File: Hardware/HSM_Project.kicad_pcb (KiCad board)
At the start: 2 copper layers, 100.6 x 113.7 mm, 105 parts, among them J1 Conn_01x02_Pin, J10 VL530X Connector, J11 VL530X Connector, J12 VL530X Connector, J13 VL530X Connector, J14 BNO085 Breakout, J16 HC-05 Breakout Board, J2 MP1584 Breakout, J4 TEENSY_4.1, J5 Conn_01x08_Pin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

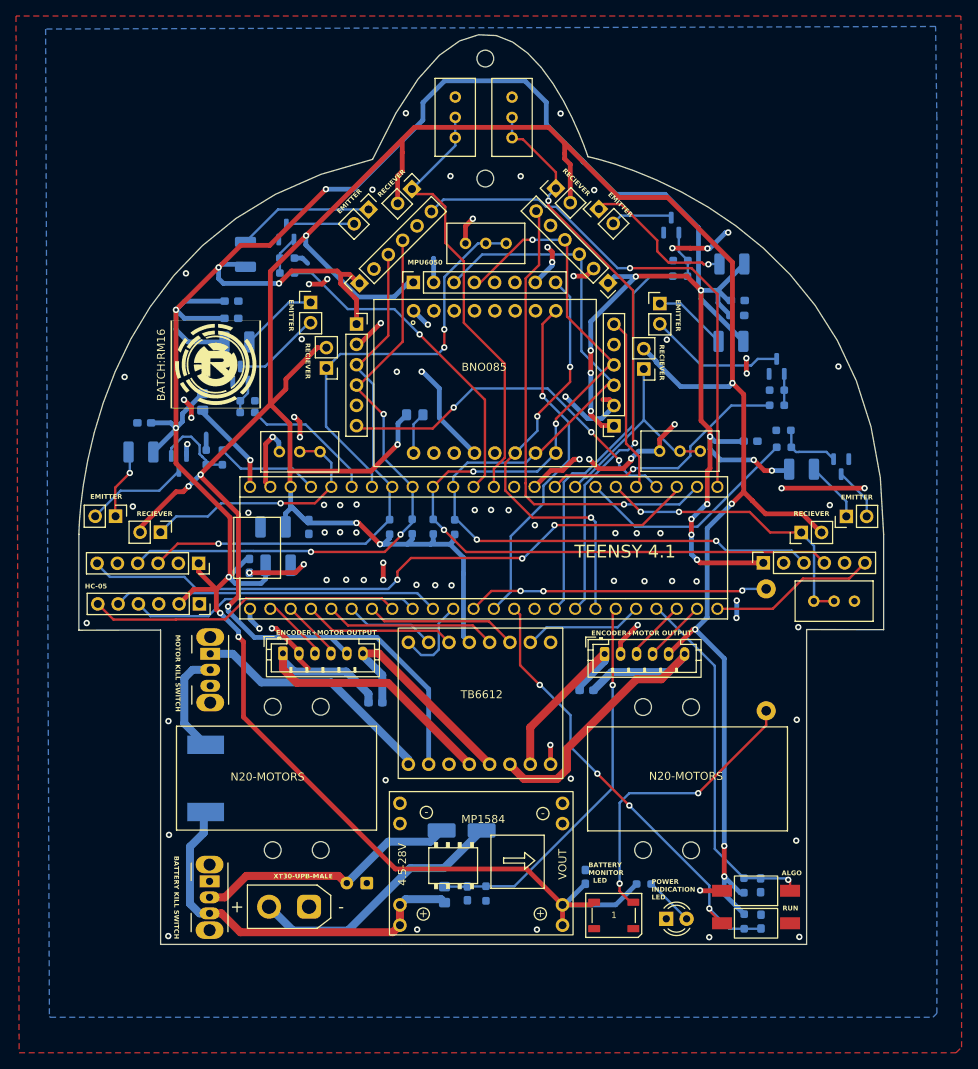
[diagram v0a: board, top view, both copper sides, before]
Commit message: Clean repository and update PCB design
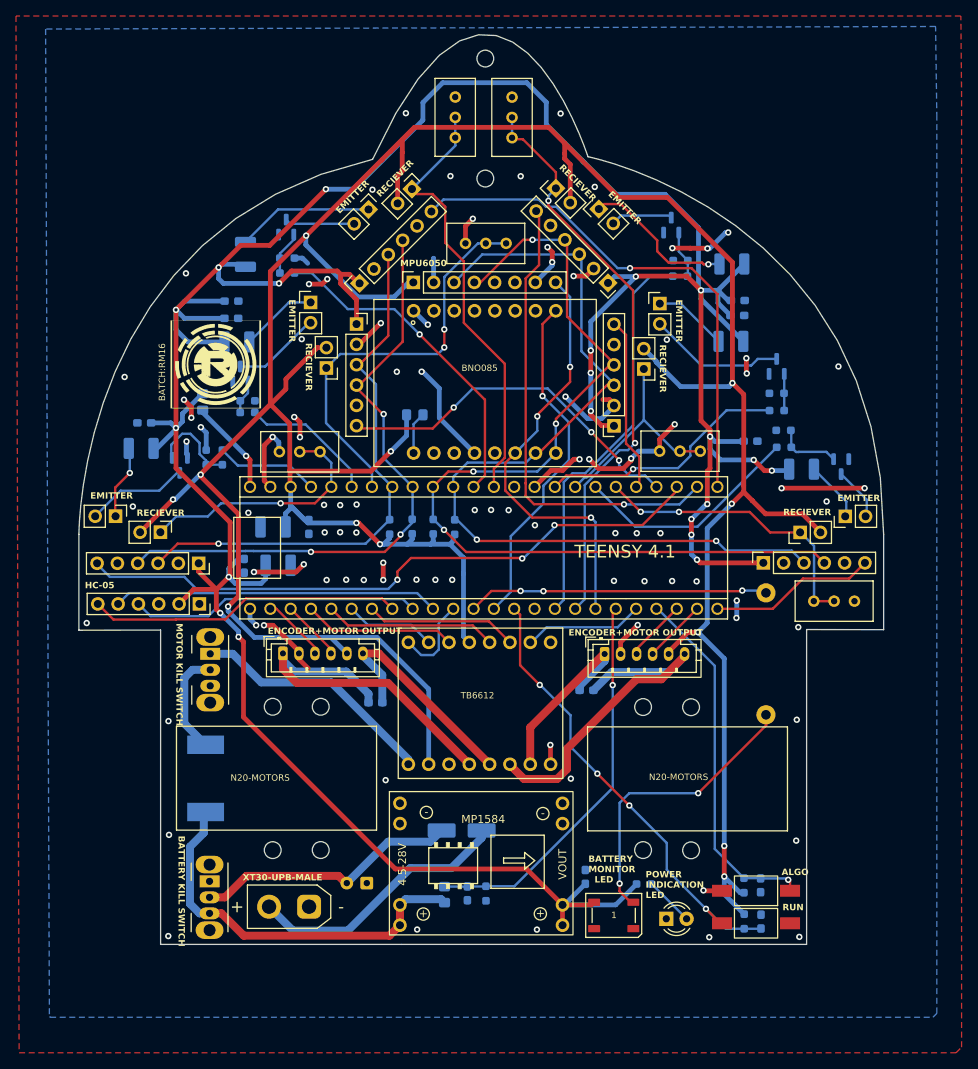
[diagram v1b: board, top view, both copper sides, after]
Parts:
- moved R19 0.66 mm to (190.2, 64.6)
- moved C4 0.65 mm to (123.6, 84.0)
- moved Q8 0.62 mm to (128.9, 41.6)
- moved R4 0.50 mm to (188.8, 87.3)
- moved R29 0.45 mm to (110.7, 69.3)
- moved R36 0.39 mm to (190.2, 62.4)
- moved Q12 0.26 mm to (115.6, 71.4)
- moved Q3 0.14 mm to (193.1, 79.8)
- moved D4 0.14 mm to (198.7, 77.8)
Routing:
- net GND: track 140.7 -> 142.2 mm, vias 89 -> 90
- net Net-(Q12-G): track 10.3 -> 11.4 mm
- net Net-(Q10-G): track 3.93 -> 4.61 mm
- net Net-(Q8-G): track 4.91 -> 5.52 mm
- net Net-(D2-A): track 33.0 -> 33.5 mm
- net /Control Unit/RUN_MODE_GPIO: track 57.7 -> 58.2 mm

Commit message: Update gitignore and PCB files
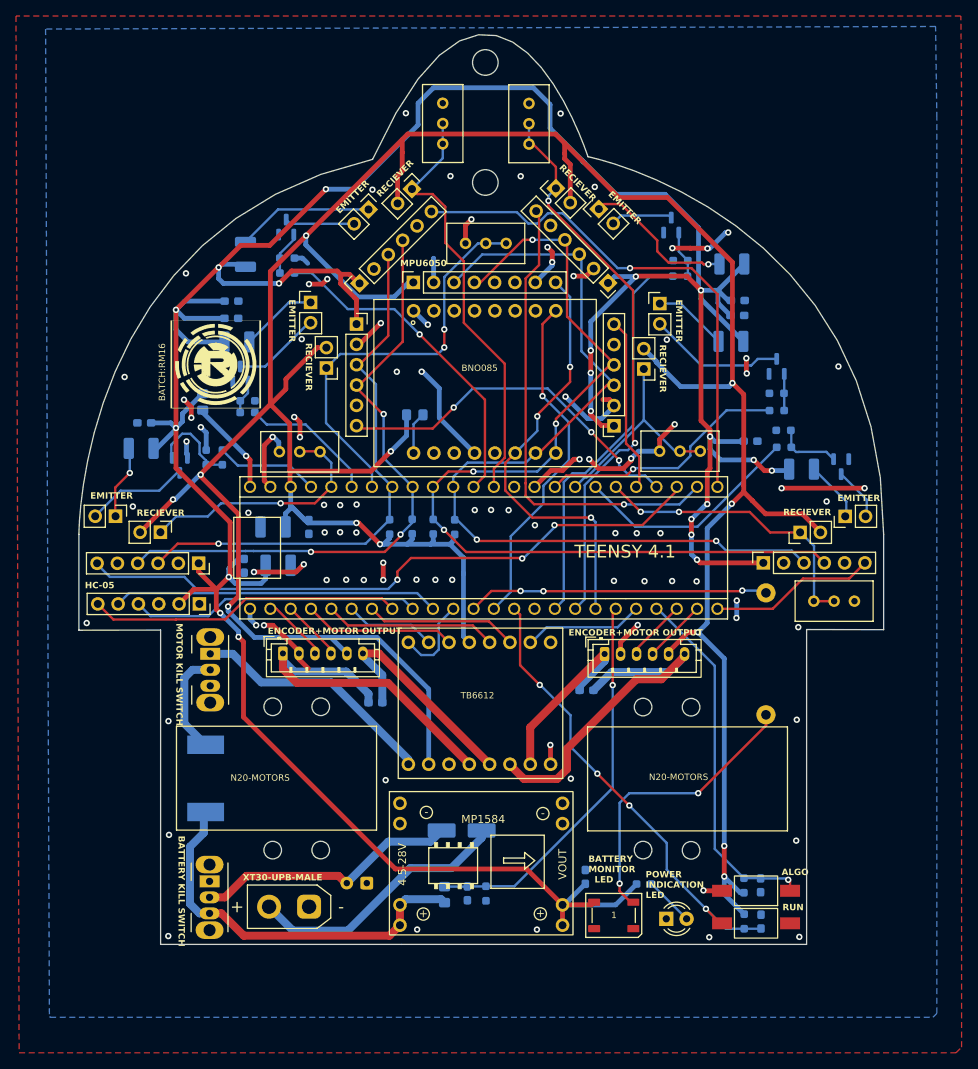
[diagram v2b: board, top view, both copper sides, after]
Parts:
- H1, H2, H3, H4, H5, H6, H7, H8: footprint MountingHole:MountingHole_2.1mm -> MountingHole:MountingHole_2.2mm_M2
- H10, H9: footprint MountingHole:MountingHole_2.1mm -> MountingHole:MountingHole_3.2mm_M3
- moved RV3 2.26 mm to (159.2, 31.2)
- moved RV2 1.74 mm to (148.4, 31.2)
- moved H10 0.49 mm to (153.8, 21.1)
- moved H9 0.49 mm to (153.8, 36.0)
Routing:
- net /Control Unit/SENS_FRONT_RIGHT: track 73.0 -> 71.3 mm
- net /Control Unit/SENS_FRONT_LEFT: track 55.1 -> 53.5 mm
- net +3.3V: track 417.6 -> 417.0 mm
